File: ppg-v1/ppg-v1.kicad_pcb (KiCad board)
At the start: 2 copper layers, 30.5 x 36.1 mm, 56 parts, among them J1 USB_microB_2040002-1, J2 Conn_01x04_Male, SW1 SW_Push, SW2 SW_Push, SW3 PCM12, U1 STM32F411CEUx, U2 MCP73831T-2ACI/OT, U3 Opamp_Dual_Generic, U4 Opamp_Dual_Generic, U5 TPS2113APW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

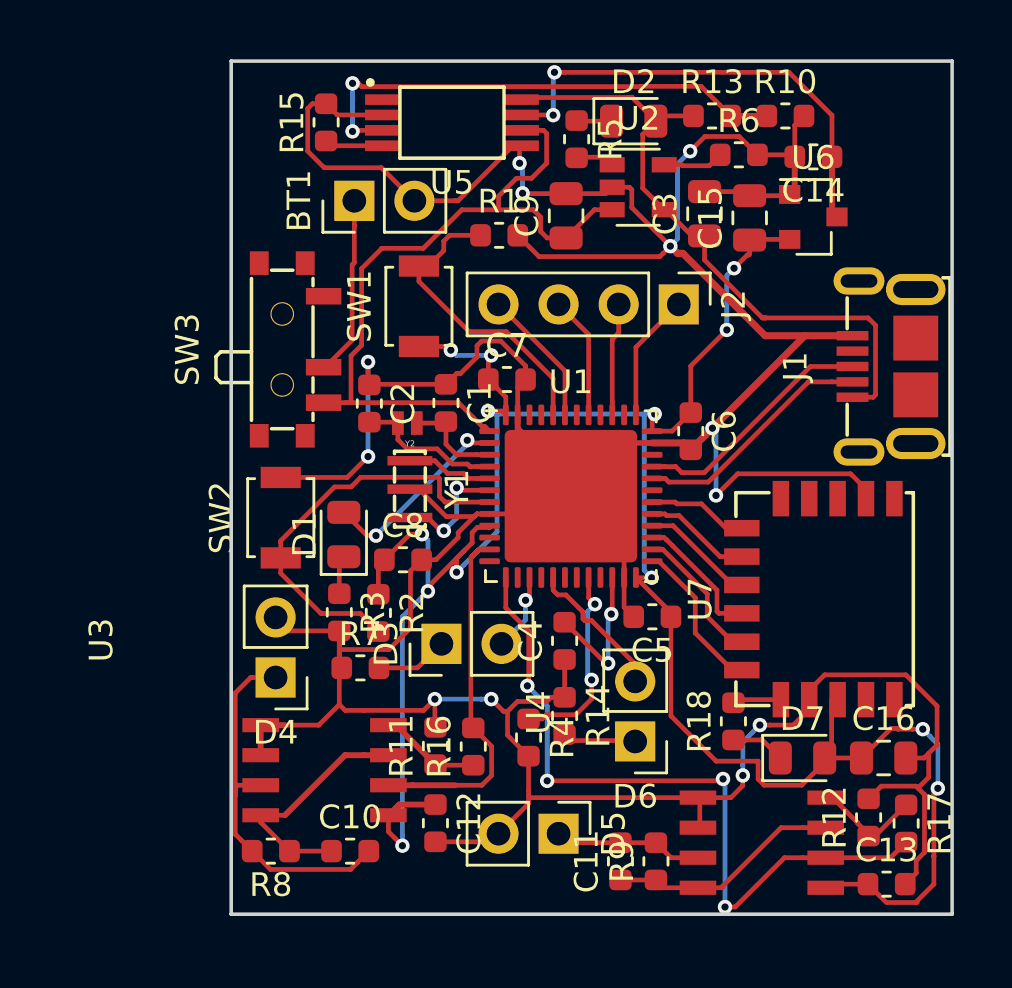
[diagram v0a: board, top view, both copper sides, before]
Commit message: more traces and edge cuts
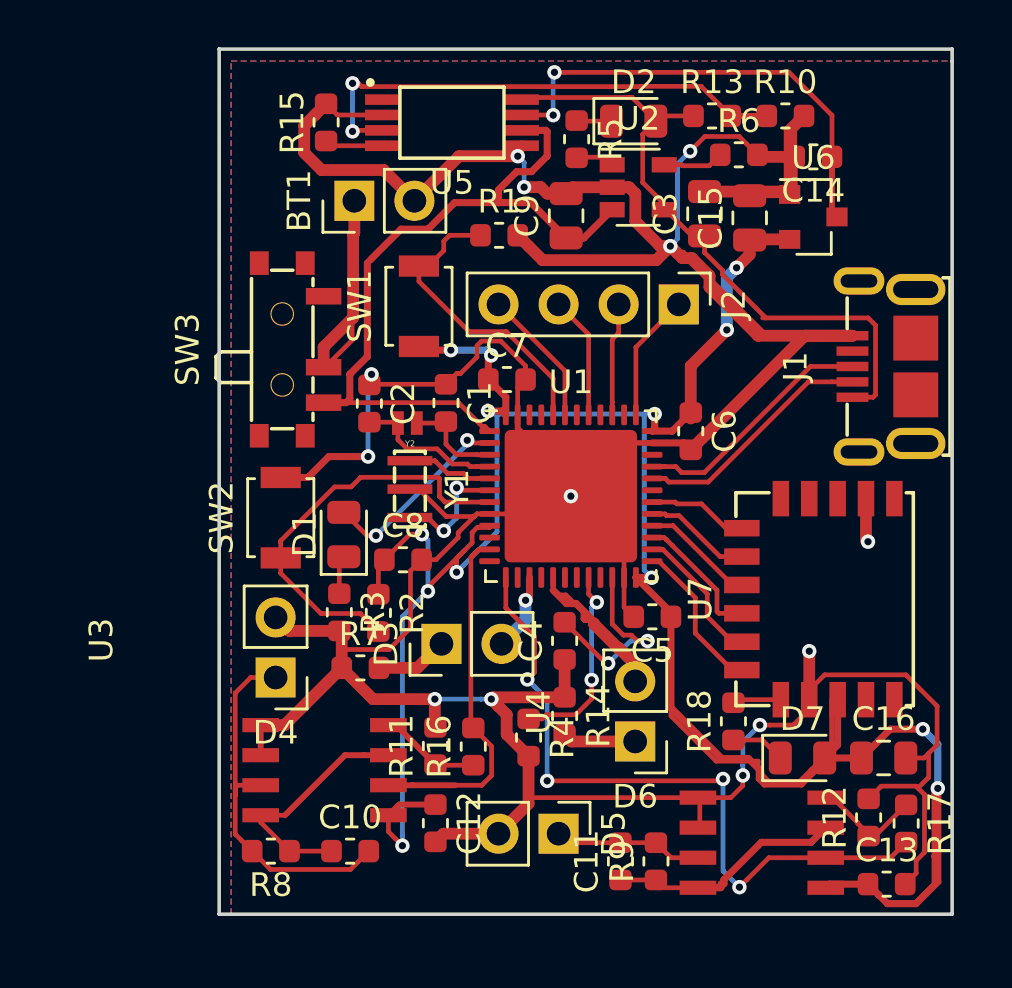
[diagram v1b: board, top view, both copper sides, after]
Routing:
- net +3V3: track 103.1 -> 129.8 mm
- net GND: track 205.3 -> 227.8 mm, vias 12 -> 13
- net Net-(BT1-Pad1): track 7.55 -> 15.1 mm
- net GreenLED: track 6.20 -> 12.1 mm
- net Net-(C4-Pad2): track 6.27 -> 8.38 mm
- net PhotoDiode2: track 31.1 -> 29.7 mm
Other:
- board size 30.5 x 36.1 mm -> 31 x 36.6 mm
- net class Default: trace_width 0.2 -> 0.3

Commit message: fix fills
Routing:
- added copper zone on F.Cu, net +3V3
- removed copper zone on F.Cu, net (none)
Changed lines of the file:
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@@
     (47 F.CrtYd user)
     (48 B.Fab user)
-    (49 F.Fab user)
+    (49 F.Fab user hide)
   )
   (setup
@@
   (segment (start 193.802 107.0285) (end 193.402 107.0285) (width 0.2) (layer F.Cu) (net 78))
   (segment (start 193.402 107.0285) (end 191.8335 105.46) (width 0.2) (layer F.Cu) (net 78))
-  (zone (net 0) (net_name "") (layer F.Cu) (hatch edge 0.508)
+  (zone (net 7) (net_name +3V3) (layer F.Cu) (hatch edge 0.508)
     (connect_pads (clearance 0.508))
     (min_thickness 0.254)
-    (fill yes (arc_segments 16) (thermal_gap 0.508) (thermal_bridge_width 0.508))
+    (fill yes (arc_segments 32) (thermal_gap 0.508) (thermal_bridge_width 0.508))
     (polygon
       (pts
-        (xy 172.212 81.28) (xy 202.692 81.28) (xy 202.692 117.348) (xy 172.212 117.348)
+        (xy 202.692 80.772) (xy 202.692 117.348) (xy 171.704 117.348) (xy 171.704 80.772)
       )
     )
@@
     (connect_pads (clearance 0.508))
     (min_thickness 0.254)
-    (fill yes (arc_segments 16) (thermal_gap 0.508) (thermal_bridge_width 0.508))
+    (fill yes (arc_segments 32) (thermal_gap 0.508) (thermal_bridge_width 0.508))
     (polygon
       (pts
-        (xy 172.212 81.28) (xy 202.692 81.28) (xy 202.692 117.348) (xy 172.212 117.348)
+        (xy 202.692 80.772) (xy 202.692 117.348) (xy 171.704 117.348) (xy 171.704 80.772)
       )
     )

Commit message: small fixes
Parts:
- moved R5 0.18 mm to (186.6, 84.6)
- moved U2 0.12 mm to (189.3, 86.6)
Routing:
- net GND: track 227.8 -> 222.8 mm
- net Net-(C14-Pad1): track 20.0 -> 23.0 mm
- net +3V3: track 129.8 -> 128.9 mm

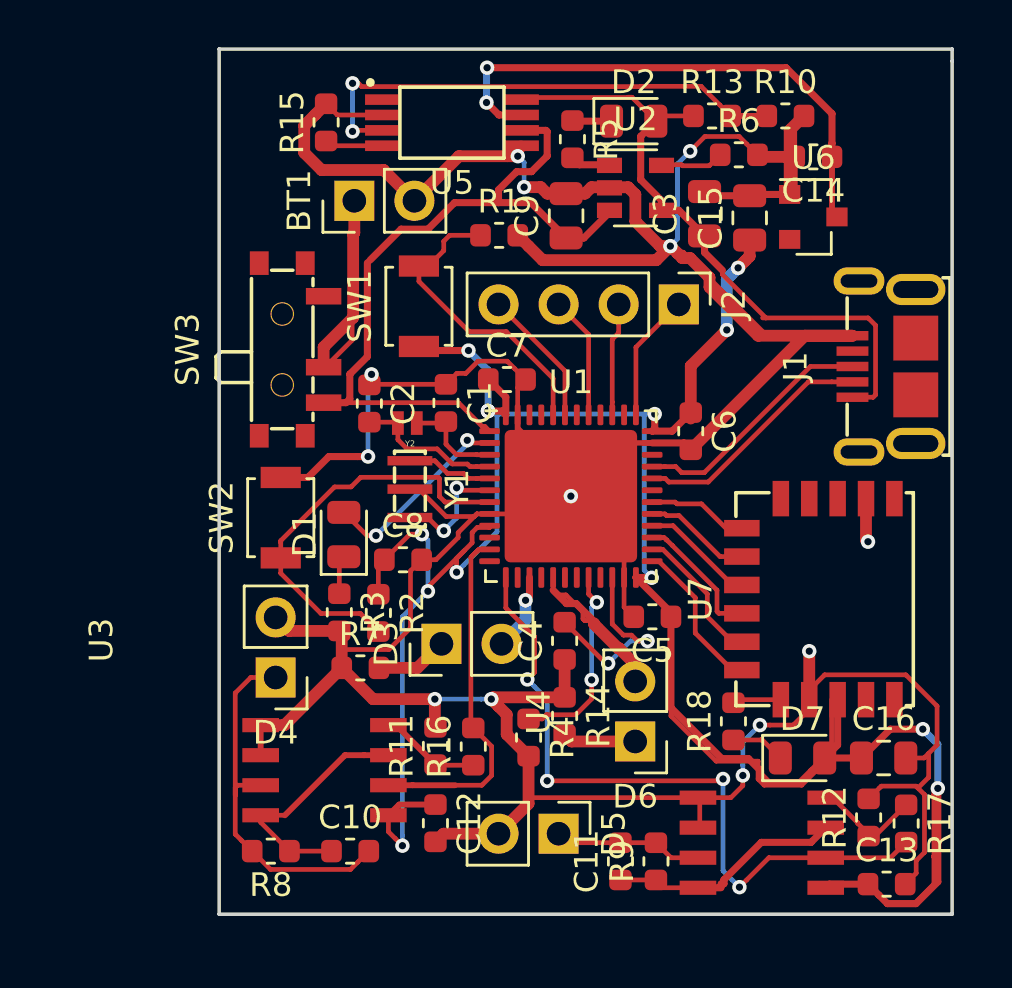
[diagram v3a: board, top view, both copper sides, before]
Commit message: replace op-amp footprints soic -> tssop
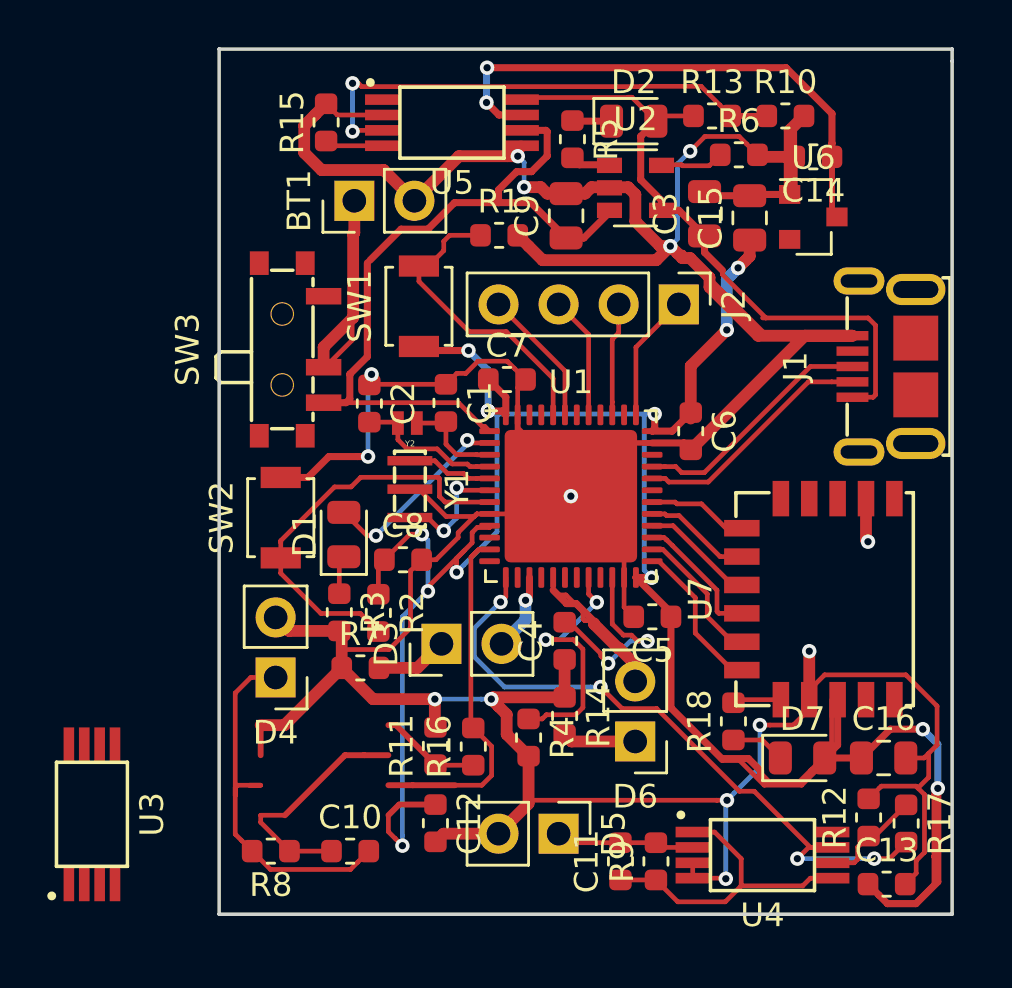
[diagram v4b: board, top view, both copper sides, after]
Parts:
- U3, U4: footprint ppg-v1:DualOpAmp -> rcpaperplane:TSSOP-8
- moved U3 7.13 mm to (166.3, 113.1)
- moved U4 3.06 mm to (194.7, 114.8), turned to 0 degrees
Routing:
- net GND: track 222.8 -> 227.0 mm, vias 13 -> 14
- net Net-(C11-Pad1): track 10.2 -> 13.9 mm
- net +3V3: track 128.9 -> 126.4 mm
- net Net-(R4-Pad1): track 8.39 -> 10.7 mm
- net PhotoDiode2: track 29.7 -> 29.2 mm

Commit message: finish arranging new footprints
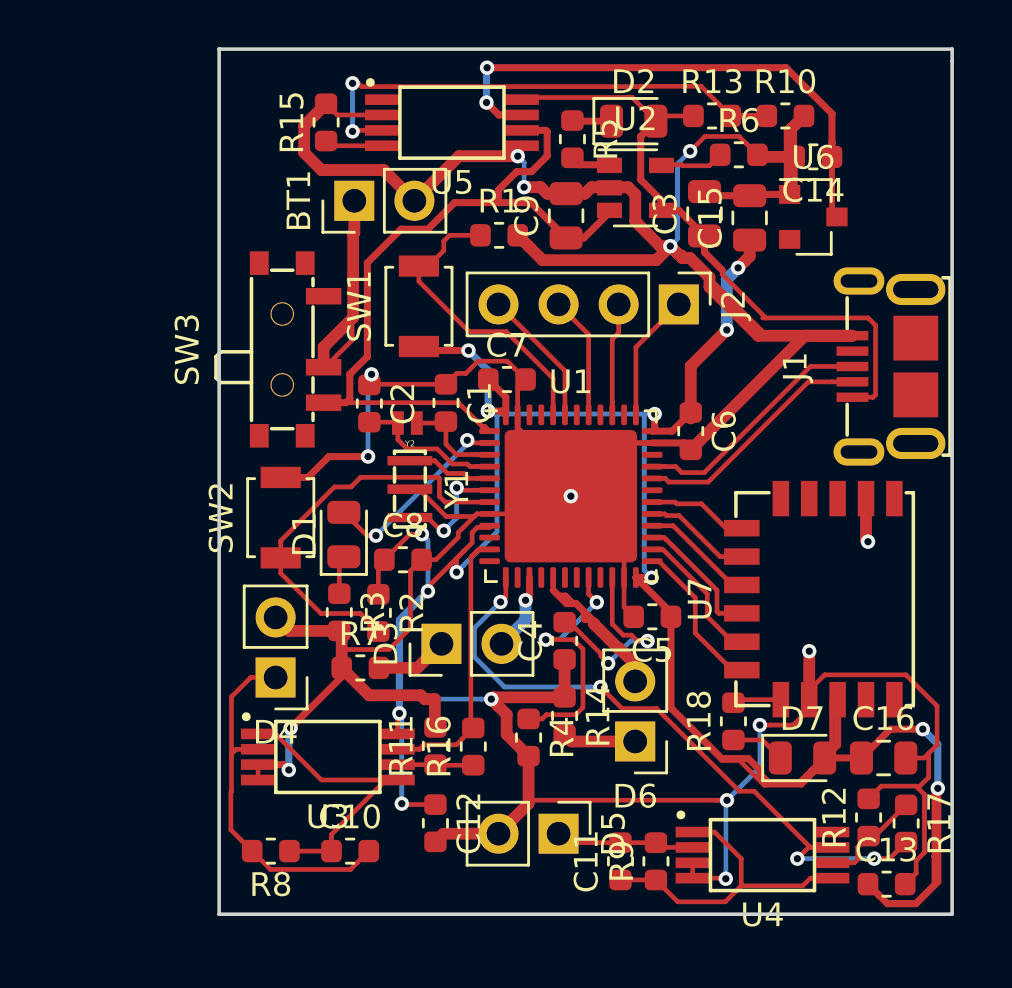
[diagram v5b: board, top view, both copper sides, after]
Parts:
- moved U3 10.3 mm to (176.3, 110.7), turned to 0 degrees
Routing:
- net PhotoDiode1: track 15.4 -> 12.1 mm
- net +3V3: track 126.4 -> 123.3 mm, vias 13 -> 14
- net Net-(C10-Pad1): track 10.2 -> 12.9 mm
- net GND: track 227.0 -> 228.6 mm, vias 14 -> 15
- net Net-(R11-Pad1): track 4.29 -> 3.21 mm

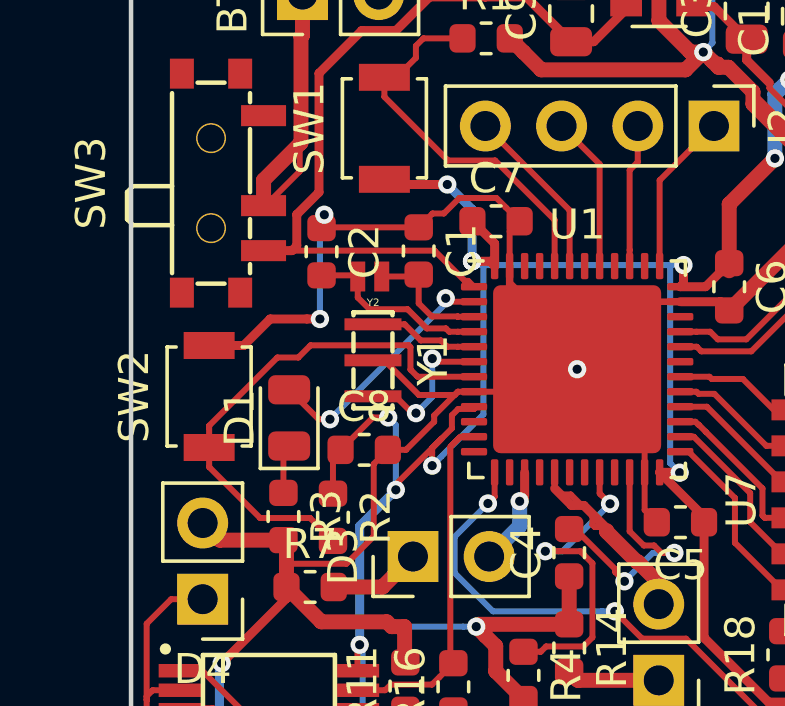
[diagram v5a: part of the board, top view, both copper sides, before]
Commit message: new footprint for resonator
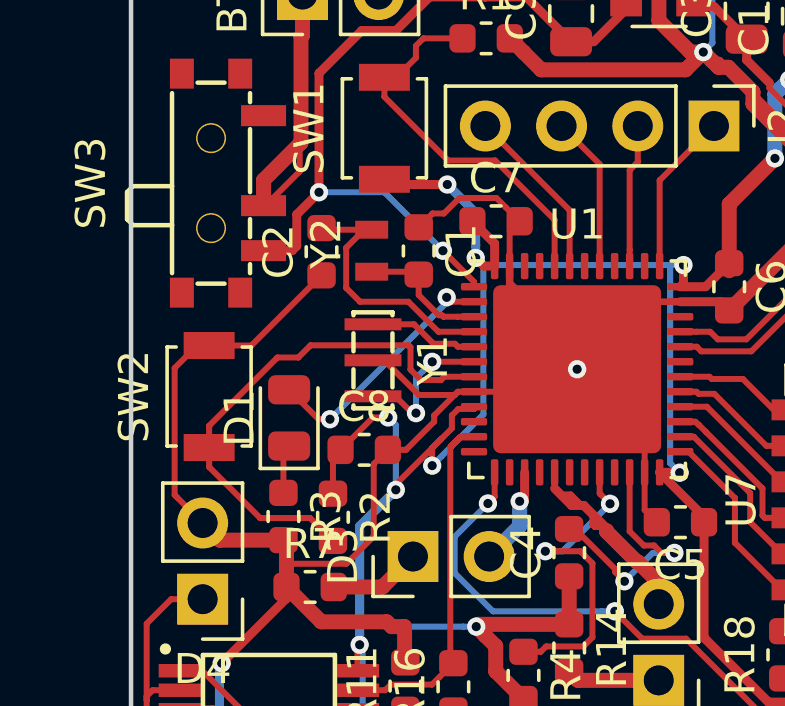
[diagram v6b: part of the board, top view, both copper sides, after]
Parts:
- Y2: footprint ppg-v1:32K28 -> ppg-v1:ECS-.327-CDX-1082
- moved Y2 0.92 mm to (179.7, 95.7), turned to 90 degrees
- turned C2 to 90 degrees
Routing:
- net Net-(C2-Pad2): track 6.27 -> 8.95 mm
- net GND: track 228.6 -> 228.9 mm, vias 15 -> 13
- net +3V3: track 123.3 -> 123.1 mm, vias 14 -> 13
- net VBAT: vias 0 -> 2

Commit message: stuff...
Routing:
- net +3V3: track 123.1 -> 124.7 mm, vias 13 -> 12
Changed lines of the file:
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@@
     (thickness 1.6)
     (drawings 5)
-    (tracks 683)
+    (tracks 684)
     (zones 0)
     (modules 56)
@@
   )
   (setup
-    (last_trace_width 0.2)
+    (last_trace_width 0.3)
     (user_trace_width 0.2)
     (trace_clearance 0.2)
@@
   (segment (start 183.136198 100.999497) (end 182.61104 100.999497) (width 0.2) (layer F.Cu) (net 7))
   (segment (start 183.136198 100.924507) (end 183.136198 100.999497) (width 0.2) (layer F.Cu) (net 7))
-  (via (at 180.5305 103.6955) (size 0.6096) (drill 0.3047) (layers F.Cu B.Cu) (net 7))
   (segment (start 182.398688 101.211849) (end 182.398688 101.646149) (width 0.2) (layer F.Cu) (net 7))
   (via (at 180.2765 101.2825) (size 0.6096) (drill 0.3047) (layers F.Cu B.Cu) (net 7))
@@
   (segment (start 182.398688 101.646149) (end 182.0545 101.990337) (width 0.2) (layer F.Cu) (net 7))
   (segment (start 182.0545 101.990337) (end 180.5305 103.514337) (width 0.2) (layer F.Cu) (net 7))
-  (via (at 181.74179 102.888838) (size 0.6096) (drill 0.3047) (layers F.Cu B.Cu) (net 7))
-  (segment (start 183.4515 96.2025) (end 183.4515 101.179128) (width 0.2) (layer B.Cu) (net 7))
-  (segment (start 182.046589 102.584039) (end 181.74179 102.888838) (width 0.2) (layer B.Cu) (net 7))
-  (segment (start 181.74179 102.457786) (end 181.74179 102.888838) (width 0.2) (layer F.Cu) (net 7))
-  (segment (start 183.4515 101.179128) (end 182.046589 102.584039) (width 0.2) (layer B.Cu) (net 7))
-  (segment (start 181.74179 102.303047) (end 181.74179 102.457786) (width 0.2) (layer F.Cu) (net 7))
-  (segment (start 182.0545 101.990337) (end 181.74179 102.303047) (width 0.2) (layer F.Cu) (net 7))
   (segment (start 201.9046 114.918639) (end 201.92392 114.899319) (width 0.2) (layer F.Cu) (net 7))
   (segment (start 197.598 110.4509) (end 197.3049 110.744) (width 0.2) (layer F.Cu) (net 7))
@@
   (segment (start 183.823698 96.237007) (end 183.467338 96.237007) (width 0.3) (layer F.Cu) (net 7))
   (segment (start 183.432831 96.2025) (end 183.193667 95.963336) (width 0.2) (layer B.Cu) (net 7))
-  (via (at 183.193667 95.963336) (size 0.6096) (drill 0.3047) (layers F.Cu B.Cu) (net 7) (status 1000000))
+  (via (at 183.193667 95.963336) (size 0.6096) (drill 0.3047) (layers F.Cu B.Cu) (net 7))
+  (segment (start 182.0545 101.990337) (end 181.74179 102.303047) (width 0.2) (layer F.Cu) (net 7))
+  (segment (start 181.74179 102.303047) (end 181.74179 102.457786) (width 0.2) (layer F.Cu) (net 7))
+  (segment (start 183.4515 101.179128) (end 182.046589 102.584039) (width 0.2) (layer B.Cu) (net 7))
+  (segment (start 181.74179 102.457786) (end 181.74179 102.888838) (width 0.2) (layer F.Cu) (net 7))
+  (segment (start 183.4515 96.2025) (end 183.4515 101.179128) (width 0.2) (layer B.Cu) (net 7))
+  (segment (start 181.337162 102.888838) (end 180.5305 103.6955) (width 0.3) (layer B.Cu) (net 7))
+  (segment (start 181.74179 102.888838) (end 181.337162 102.888838) (width 0.3) (layer B.Cu) (net 7))
+  (segment (start 181.74179 102.888838) (end 182.046589 102.584039) (width 0.3) (layer B.Cu) (net 7))
+  (via (at 181.74179 102.888838) (size 0.6096) (drill 0.3047) (layers F.Cu B.Cu) (net 7))
   (segment (start 184.879332 87.264832) (end 183.515 87.264832) (width 0.3) (layer F.Cu) (net 8))
   (segment (start 186.3725 88.758) (end 184.879332 87.264832) (width 0.3) (layer F.Cu) (net 8))
